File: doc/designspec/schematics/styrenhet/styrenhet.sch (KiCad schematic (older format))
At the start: 4 parts, among them IC1 ATMEGA1284P-P, U1 IQEXO-3, U2 Terminator-CTRL, U3 USB-UART

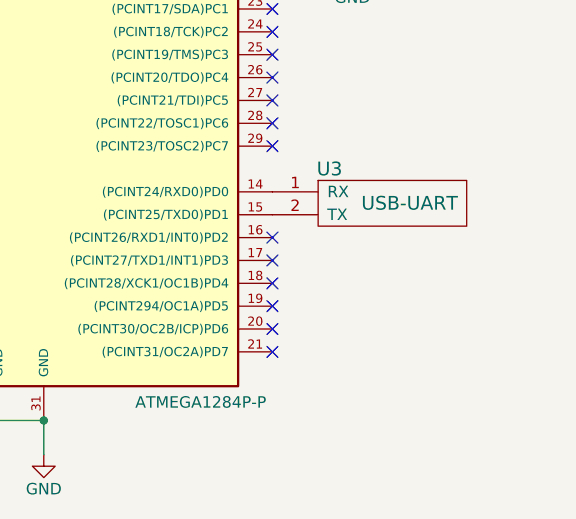
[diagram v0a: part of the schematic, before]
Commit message: Add todo for servo
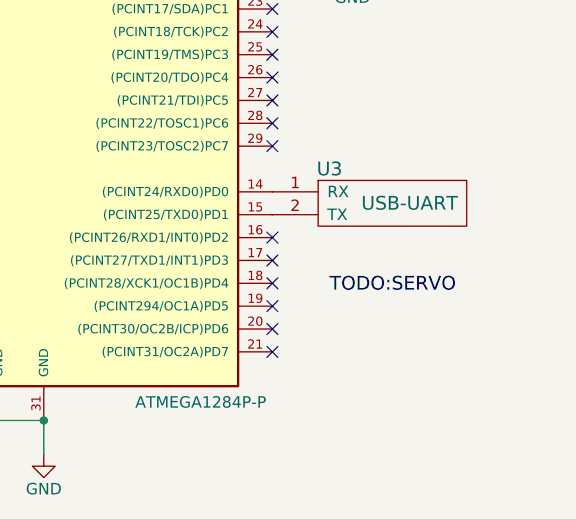
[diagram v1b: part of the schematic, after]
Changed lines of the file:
@@
 LIBS:contrib
 LIBS:valves
-LIBS:styrenhet-cache
+LIBS:tsea29
 EELAYER 25 0
 EELAYER END
@@
 	1    0    0    -1
 $EndComp
+Text Label 6000 5150 0    60   ~ 0
+TODO:SERVO
 $EndSCHEMATC

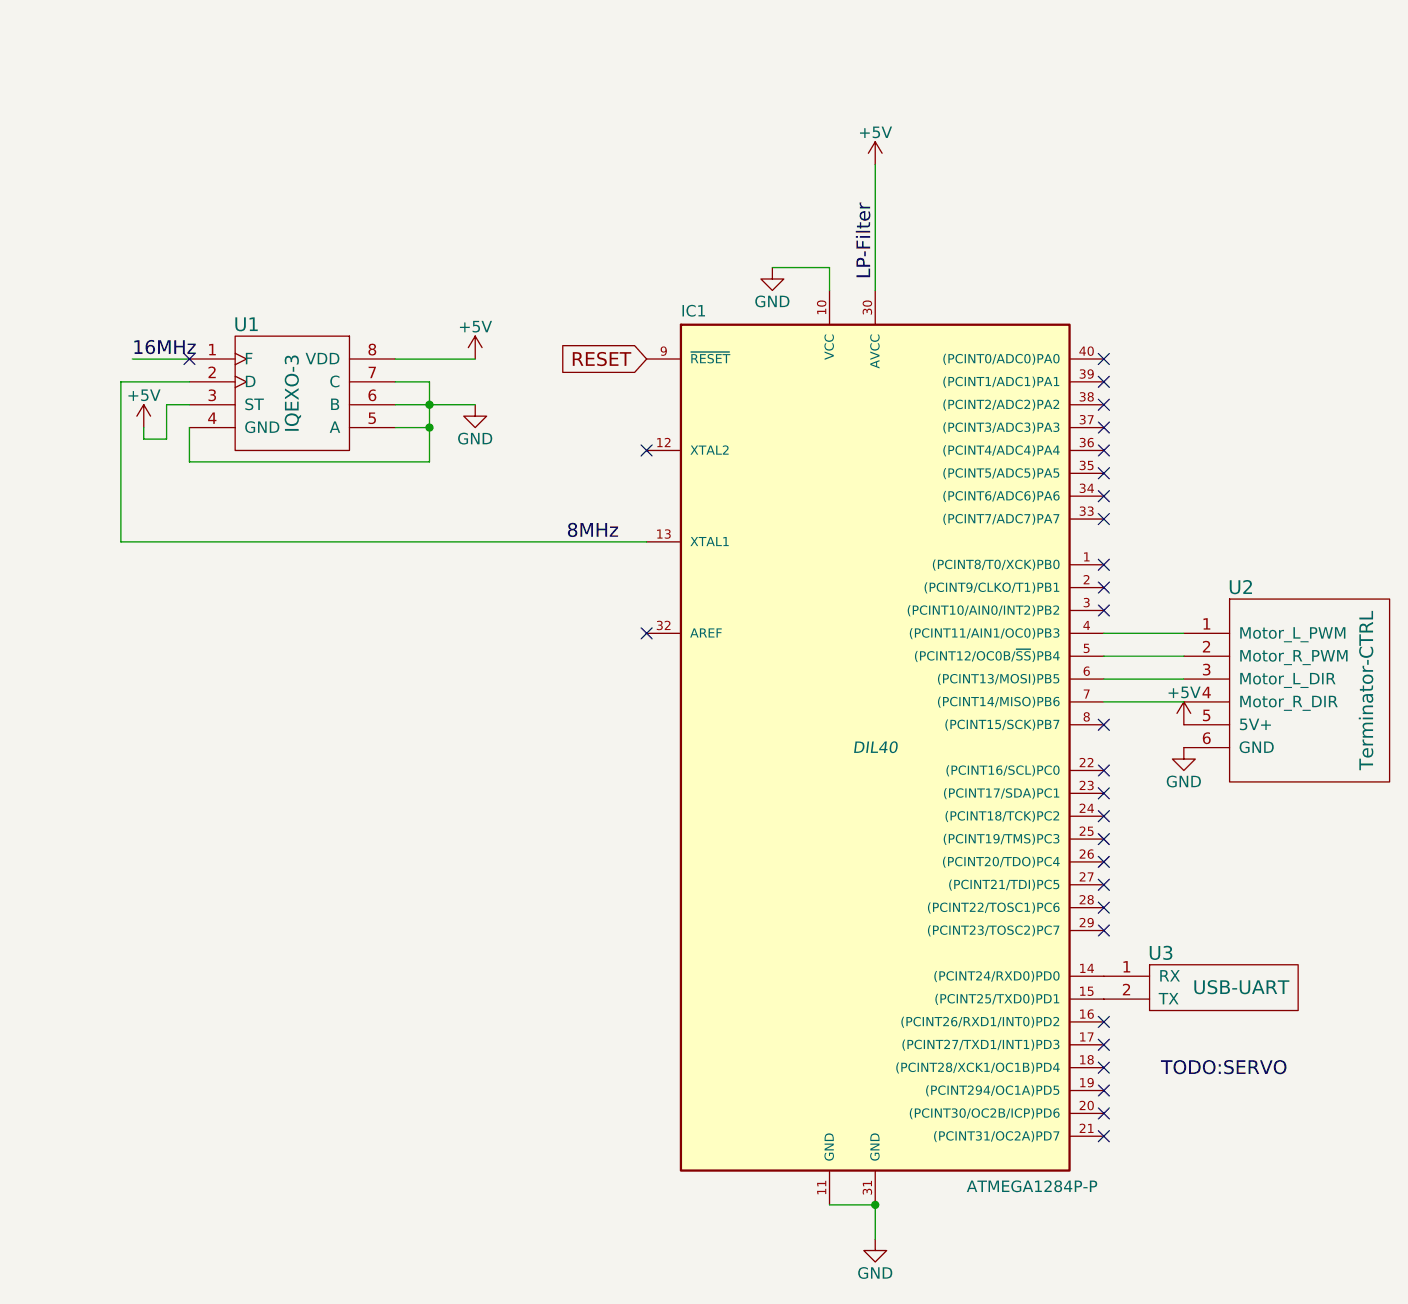
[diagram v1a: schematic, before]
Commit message: Add servo to styrenhet
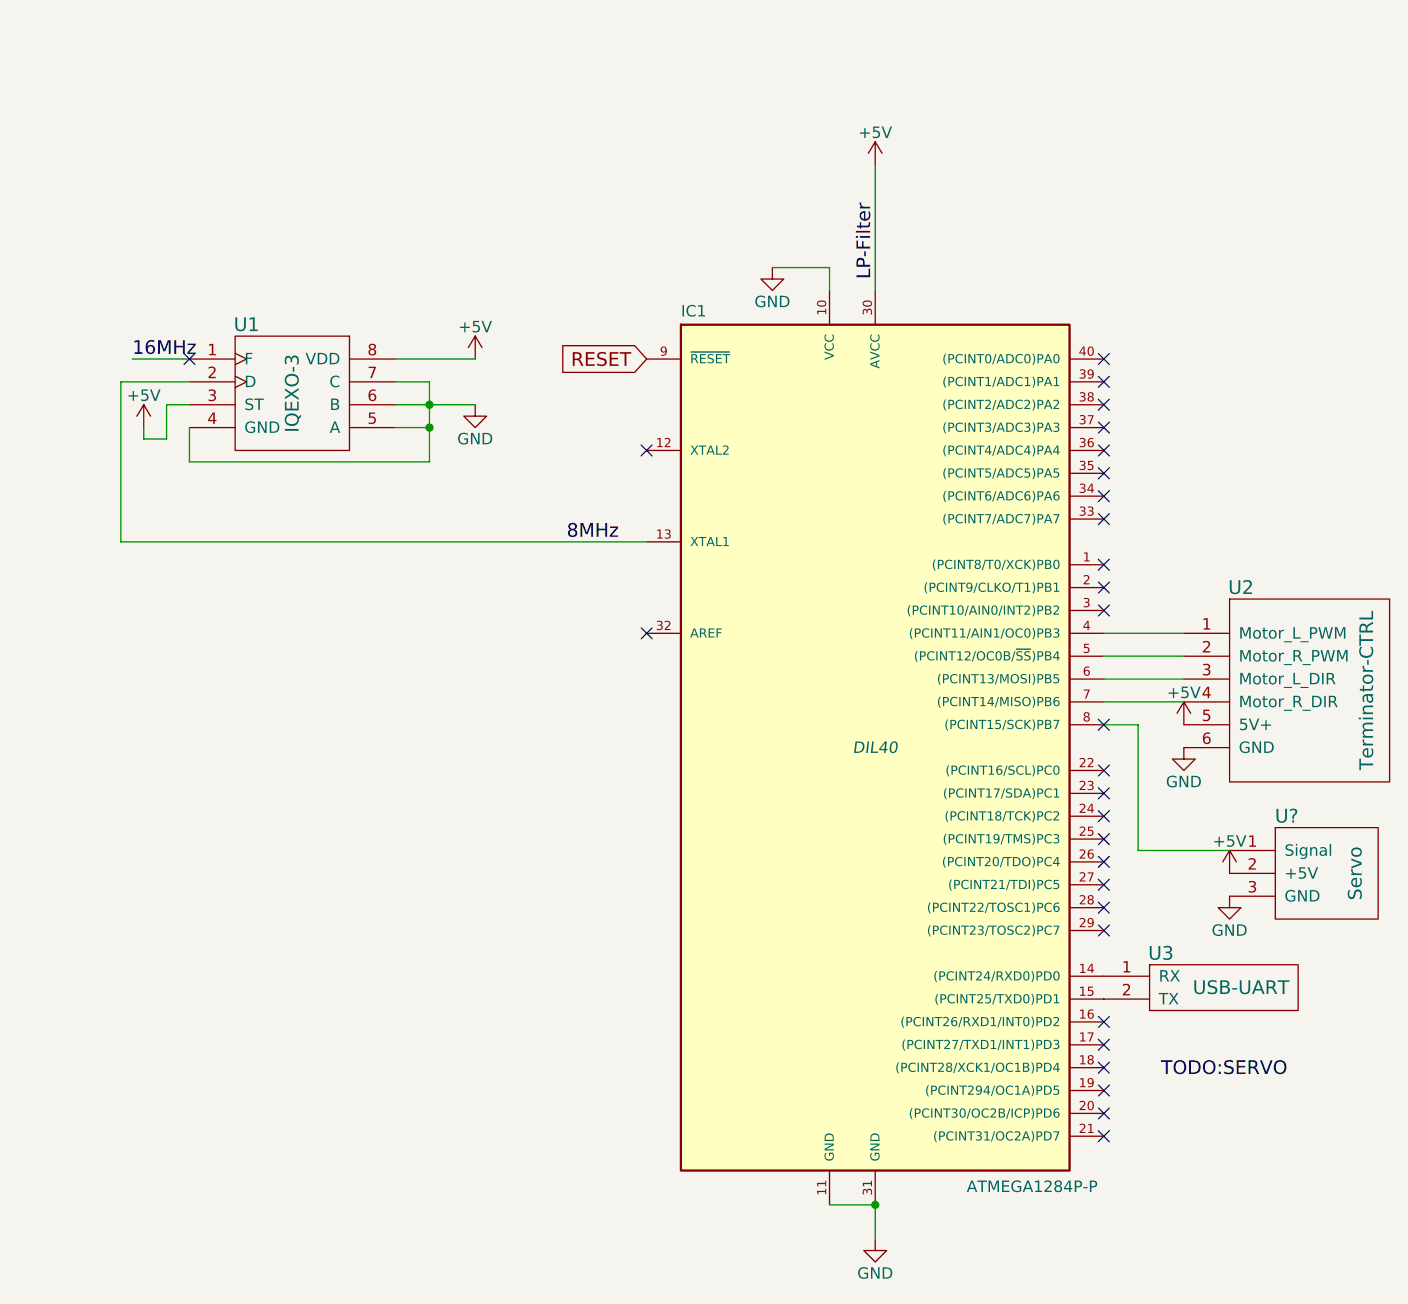
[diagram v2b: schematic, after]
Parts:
- added U?: Servo, symbol Servo
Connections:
- net +5V: now also U?.2 (+5V)
- net GND: now also U?.3 (GND)
- net at IC1.8 ((PCINT15/SCK)PB7): now also U?.1 (Signal)
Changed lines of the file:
@@
 LIBS:valves
 LIBS:tsea29
+LIBS:styrenhet-cache
 EELAYER 25 0
 EELAYER END
@@
 	2800 2300 2650 2300
 Wire Wire Line
-	2800 2100 2800 2450
-Wire Wire Line
-	2650 2200 3000 2200
+	2800 2100 2800 2200
+Wire Wire Line
+	2800 2200 2800 2300
+Wire Wire Line
+	2800 2300 2800 2450
+Wire Wire Line
+	2650 2200 2800 2200
+Wire Wire Line
+	2800 2200 3000 2200
 Connection ~ 2800 2200
 Wire Wire Line
@@
 Text Label 6000 5150 0    60   ~ 0
 TODO:SERVO
+Wire Wire Line
+	5750 3600 5900 3600
+Wire Wire Line
+	5900 3600 5900 4150
+Wire Wire Line
+	5900 4150 6300 4150
+$Comp
+L Servo U?
+U 1 1 57FFAFE2
+P 6850 4250
+F 0 "U?" H 6550 4500 60  0000 C CNN
+F 1 "Servo" V 6850 4250 60  0000 C CNN
+F 2 "" H 6850 4250 60  0001 C CNN
+F 3 "" H 6850 4250 60  0001 C CNN
+	1    6850 4250
+	1    0    0    -1
+$EndComp
+$Comp
+L +5V #PWR?
+U 1 1 57FFB033
+P 6300 4250
+F 0 "#PWR?" H 6300 4100 50  0001 C CNN
+F 1 "+5V" H 6300 4390 50  0000 C CNN
+F 2 "" H 6300 4250 50  0000 C CNN
+F 3 "" H 6300 4250 50  0000 C CNN
+	1    6300 4250
+	1    0    0    -1
+$EndComp
+$Comp
+L GND #PWR?
+U 1 1 57FFB05B
+P 6300 4350
+F 0 "#PWR?" H 6300 4100 50  0001 C CNN
+F 1 "GND" H 6300 4200 50  0000 C CNN
+F 2 "" H 6300 4350 50  0000 C CNN
+F 3 "" H 6300 4350 50  0000 C CNN
+	1    6300 4350
+	1    0    0    -1
+$EndComp
 $EndSCHEMATC

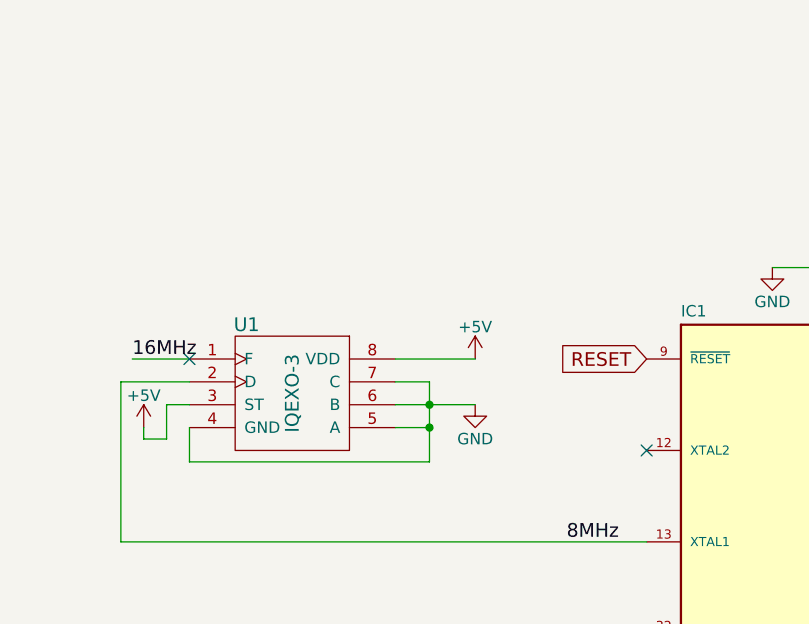
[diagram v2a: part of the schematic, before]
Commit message: Add reset to styrenhet
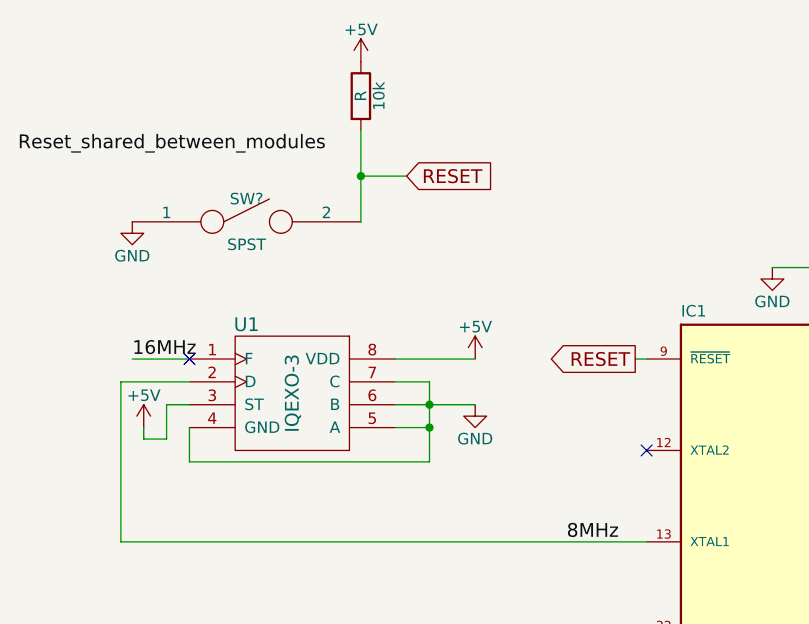
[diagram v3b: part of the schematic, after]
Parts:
- added 10k: R, symbol R
- added SW?: SPST, symbol SPST
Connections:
- net +5V: now also 10k.1
- net GND: now also SW?.1
- net RESET: now also 10k.2, SW?.2
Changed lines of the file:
@@
 	2800 2300 2650 2300
 Wire Wire Line
-	2800 2100 2800 2200
-Wire Wire Line
-	2800 2200 2800 2300
-Wire Wire Line
-	2800 2300 2800 2450
-Wire Wire Line
-	2650 2200 2800 2200
-Wire Wire Line
-	2800 2200 3000 2200
+	2800 2100 2800 2450
+Wire Wire Line
+	2650 2200 3000 2200
 Connection ~ 2800 2200
 Wire Wire Line
@@
 	1    0    0    -1
 $EndComp
-Text GLabel 3750 2000 0    60   Input ~ 0
-RESET
 NoConn ~ 5750 2000
 NoConn ~ 5750 2100
@@
 	1    0    0    -1
 $EndComp
+$Comp
+L SPST SW?
+U 1 1 58011D2C
+P 2000 1400
+F 0 "SW?" H 2000 1500 50  0000 C CNN
+F 1 "SPST" H 2000 1300 50  0000 C CNN
+F 2 "" H 2000 1400 50  0000 C CNN
+F 3 "" H 2000 1400 50  0000 C CNN
+	1    2000 1400
+	1    0    0    -1
+$EndComp
+$Comp
+L R 10k
+U 1 1 58011D8D
+P 2500 850
+F 0 "10k" V 2580 850 50  0000 C CNN
+F 1 "R" V 2500 850 50  0000 C CNN
+F 2 "" V 2430 850 50  0000 C CNN
+F 3 "" H 2500 850 50  0000 C CNN
+	1    2500 850
+	1    0    0    -1
+$EndComp
+$Comp
+L +5V #PWR?
+U 1 1 58011E06
+P 2500 700
+F 0 "#PWR?" H 2500 550 50  0001 C CNN
+F 1 "+5V" H 2500 840 50  0000 C CNN
+F 2 "" H 2500 700 50  0000 C CNN
+F 3 "" H 2500 700 50  0000 C CNN
+	1    2500 700
+	1    0    0    -1
+$EndComp
+$Comp
+L GND #PWR?
+U 1 1 58011E31
+P 1500 1400
+F 0 "#PWR?" H 1500 1150 50  0001 C CNN
+F 1 "GND" H 1500 1250 50  0000 C CNN
+F 2 "" H 1500 1400 50  0000 C CNN
+F 3 "" H 1500 1400 50  0000 C CNN
+	1    1500 1400
+	1    0    0    -1
+$EndComp
+Wire Wire Line
+	2500 1000 2500 1400
+Connection ~ 2500 1200
+Text Label 1000 1100 0    60   ~ 0
+Reset_shared_between_modules
+Text GLabel 2700 1200 2    60   Input ~ 0
+RESET
+Wire Wire Line
+	2700 1200 2500 1200
+Text GLabel 3700 2000 0    60   Output ~ 0
+RESET
+Wire Wire Line
+	3700 2000 3750 2000
 $EndSCHEMATC
